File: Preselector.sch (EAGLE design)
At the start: 167 parts, among them IC4 TPS7A8101DRB, IC58 LMZ31707RVQ, Q2 FDV303N, X1 0733660061, X10 0733660061, X11 0733660061, X12 0733660061, X13 0733660061, X14 0733660061, X15 0733660061, X16 0733660061, X17 0733660061, X18 0733660061, X19 0733660061, X2 0733660061, X20 0733660061, X21 0733660061, X22 0733660061, X23 0733660061, X24 0733660061, X25 0733660061, X26 0733660061, X27 0733660061, X28 0733660061, X29 0733660061, X3 0733660061, X30 0733660061, X31 0733660061, X32 0733660061, X4 0733660061, X5 0733660061, X6 0733660061, X7 0733660061, X8 0733660061, X9 0733660061

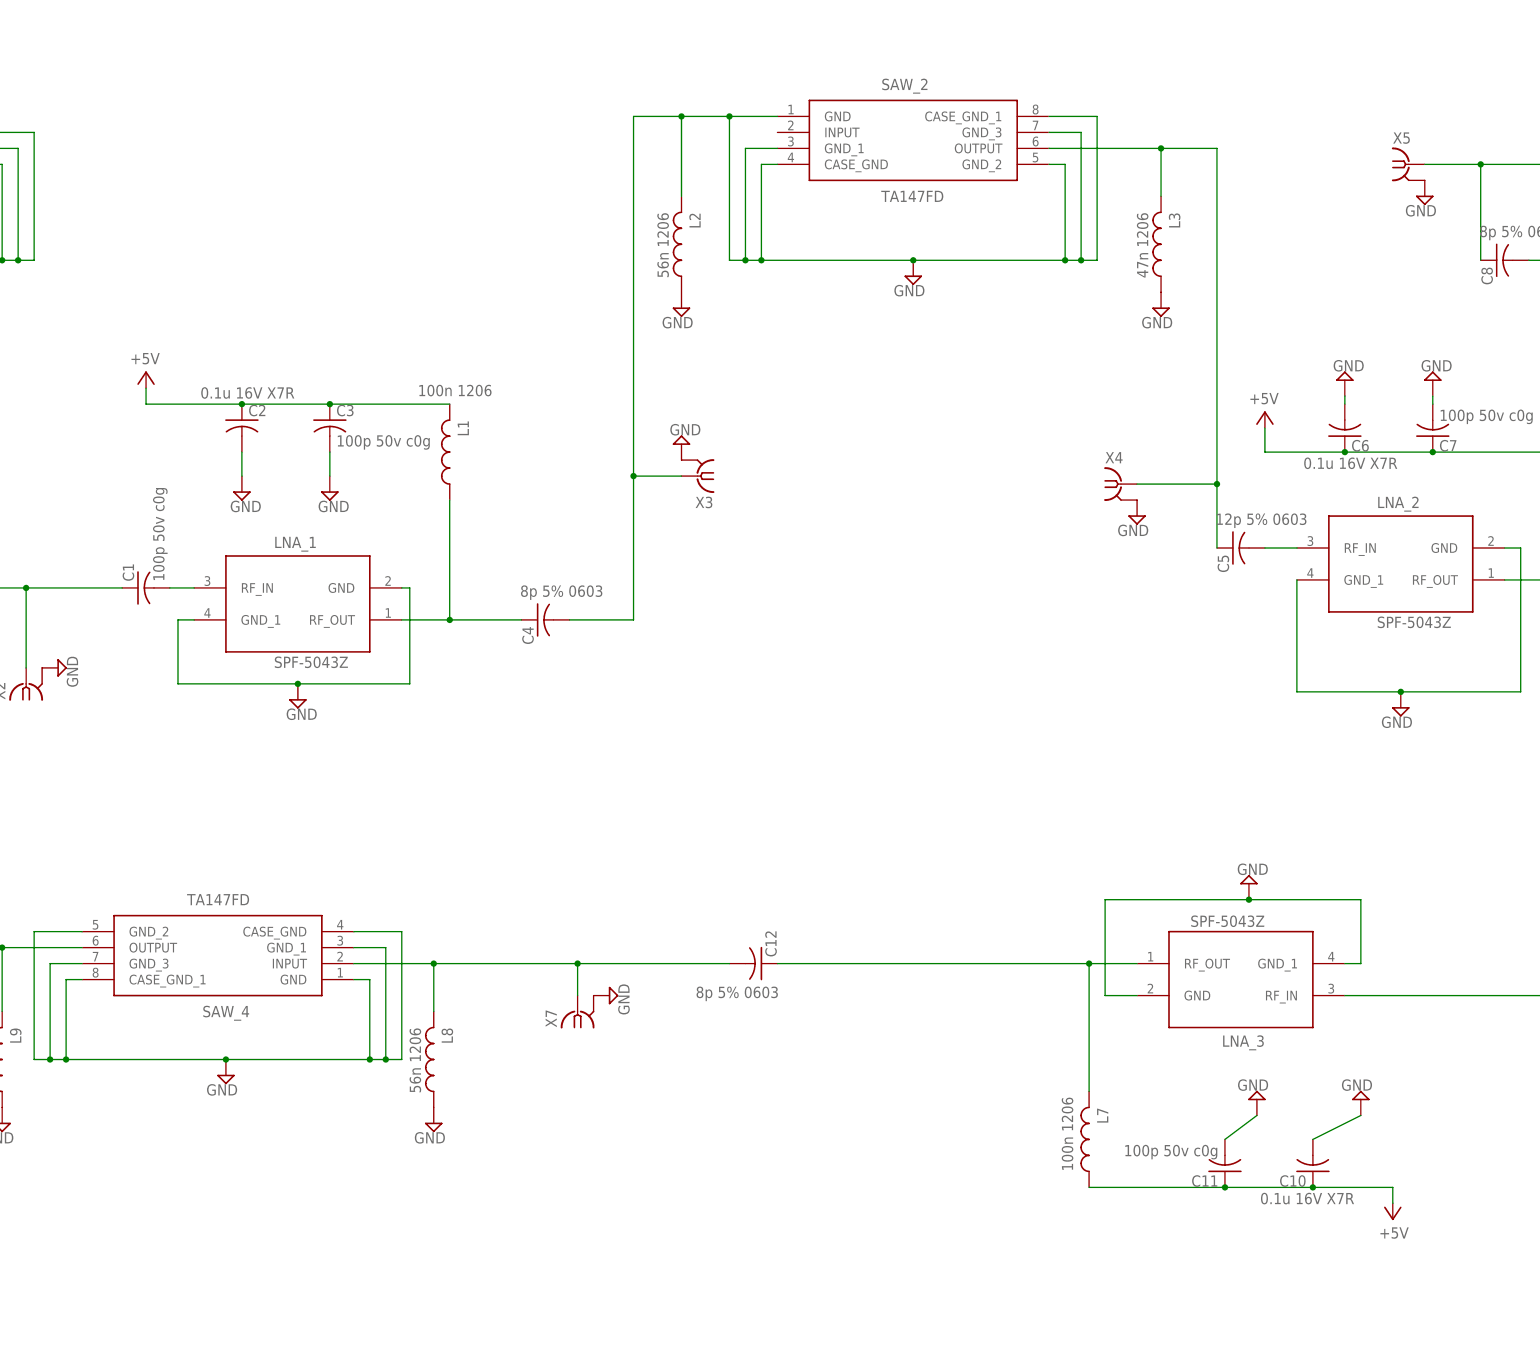
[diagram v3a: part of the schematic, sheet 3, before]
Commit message: Fixed all ERC errors
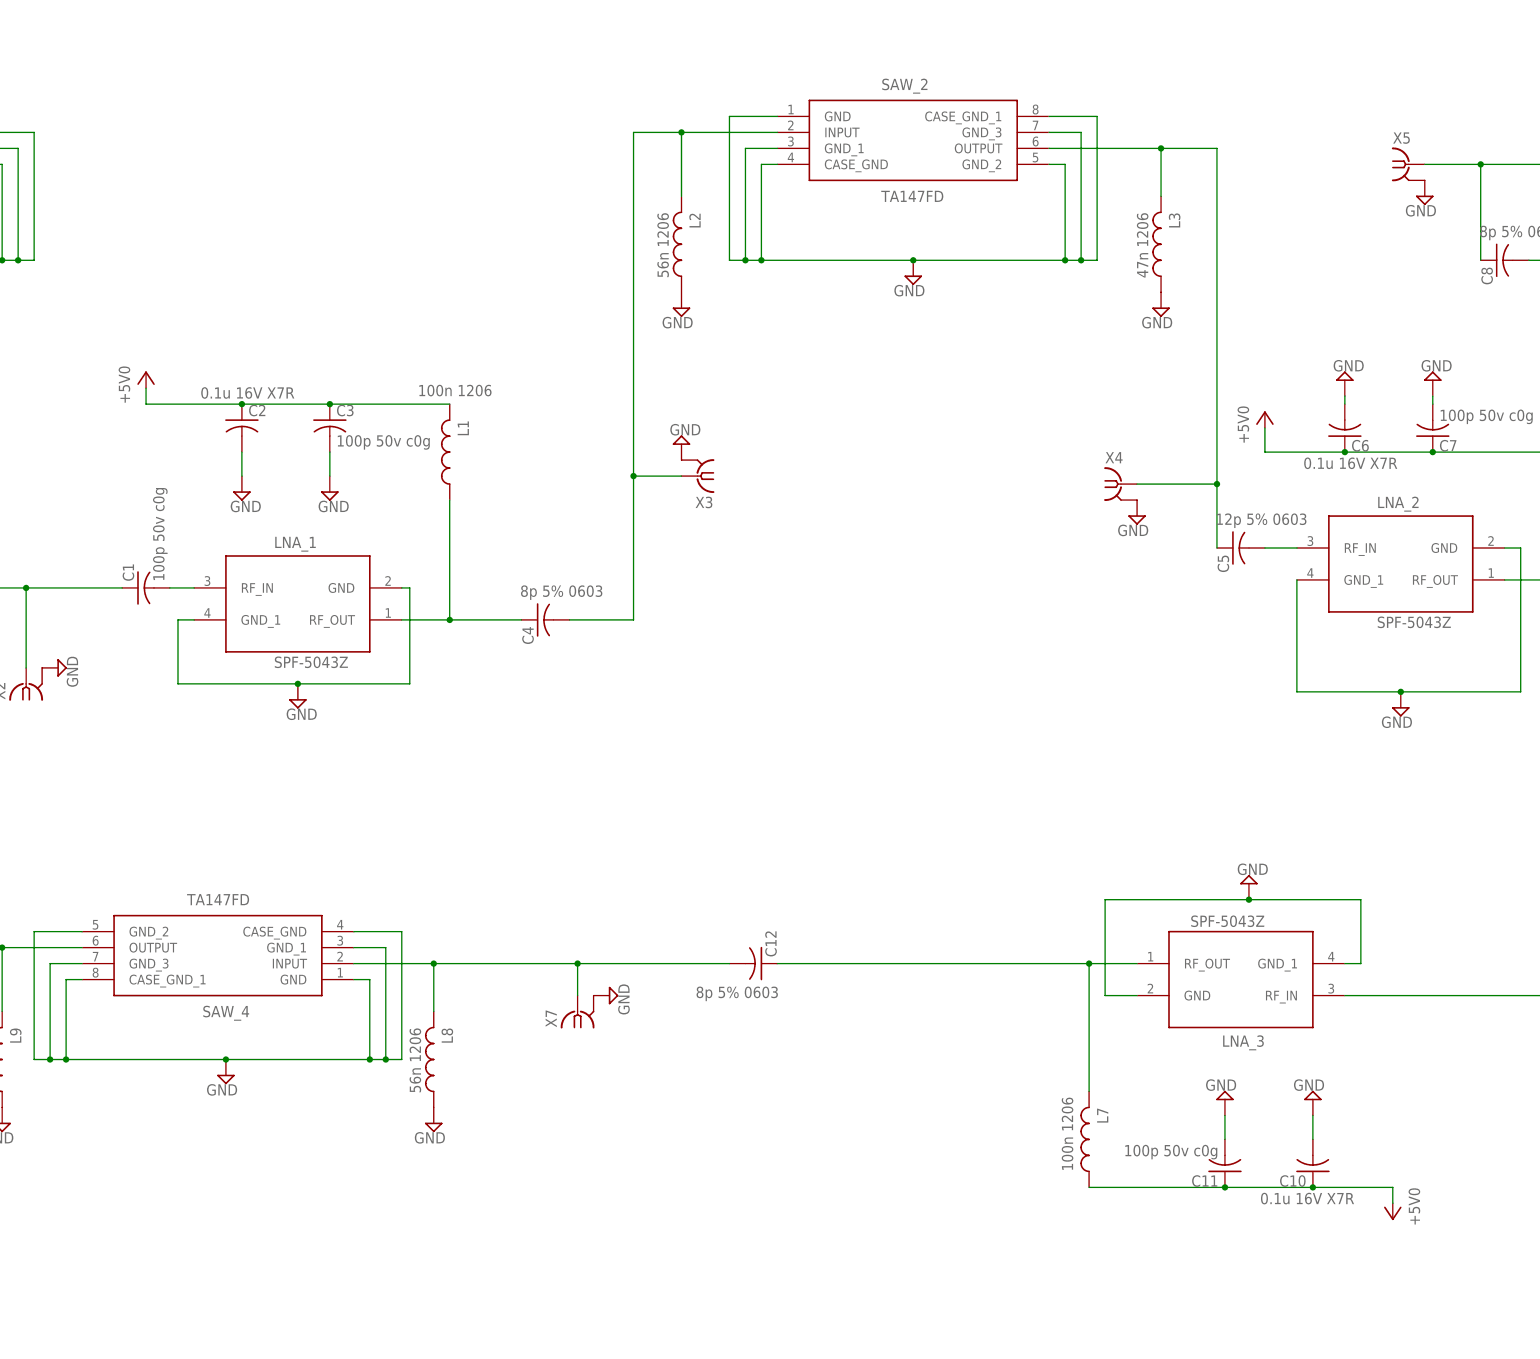
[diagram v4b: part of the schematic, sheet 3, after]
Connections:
- net +5V renamed +5V0
- net 1.25M_RF_IN1 renamed LNA_6_IN
- net 1.25M_RF_IN3 renamed LNA_5_IN
- net 2M_RF_IN1 renamed SAW_9_IN
- net 2M_RF_IN10 renamed SAW_10_OUT
- net 2M_RF_IN11 renamed SAW_11_12_RF
- net 2M_RF_IN14 renamed SAW+6_OUT
- net 2M_RF_IN15 renamed SAW_7_IN
- net 2M_RF_IN16 renamed SAW_7_8_RF
- net 2M_RF_IN17 renamed LNA_1_OUT
- net 2M_RF_IN19 renamed LNA_2_OUT
- net 2M_RF_IN2 renamed LNA_4_IN
- net 2M_RF_IN20 renamed LNA_3_OUT
- net 2M_RF_IN3 renamed 1.25_RF_OUT
- net 2M_RF_IN5 renamed SAW_10_IN
- net 2M_RF_IN6 renamed LNA_8_IN
- net 2M_RF_IN7 renamed SAW_11_IN
- net 2M_RF_IN8 renamed LNA_9_IN
- net 2M_RF_IN9 renamed SAW_9_OUT
- net 2M_RF_IN_14 renamed LNA_1_IN
- net 2M_RF_IN_4 renamed SAW_2_OUT
- net 2M_RF_IN_7 renamed SAW_3_IN
- net 2M_RF_IN_9 renamed LNA_3_IN
- net GND5 renamed LNA_8_OUT
- net GND6 renamed LNA_9_OUT
- net N$11 renamed SAW_3_OUT
- net N$13 renamed LNA_6_OUT
- net N$7 renamed 70CM_RF_OUT
- net N$9 renamed LNA_2_IN
- removed net 2M_RF_IN4: C26.1, C26.2, LNA_7.RF_IN, X17G$1.1
- new net 2M_RF_OUT: C13.2, X8G$1.1
- new net LNA_7_IN: C26.2, LNA_7.RF_IN
- new net LNA_7_OUT: C29.1, L13.1, LNA_7.RF_OUT
- new net SAW_2_IN: C4.2, L2.2, SAW_2.INPUT, X3G$1.1
- new net SAW_6_IN: C21.2, SAW_6.INPUT, X12G$1.1
- net 1.25M_RF_IN: no longer C21.1, L11.1, LNA_5.RF_OUT
- net 2M_RF_IN: no longer C13.2, X8G$1.1
- net 70CM_RF_IN: now also C26.1, X17G$1.1; no longer C29.1, L13.1, LNA_7.RF_OUT
- net GND: no longer C4.2, L2.2, X3G$1.1
- net LNA_5_OUT: now also C21.1, L11.1, LNA_5.RF_OUT; no longer C21.2, SAW_6.INPUT, X12G$1.1
- net SAW_4_IN: now also C12.2, L8.2, SAW_4.INPUT, X7G$1.1; no longer C13.1, L9.2, SAW_4.OUTPUT
- net SAW_4_OUT: now also C13.1, L9.2, SAW_4.OUTPUT; no longer C12.2, L8.2, SAW_4.INPUT, X7G$1.1

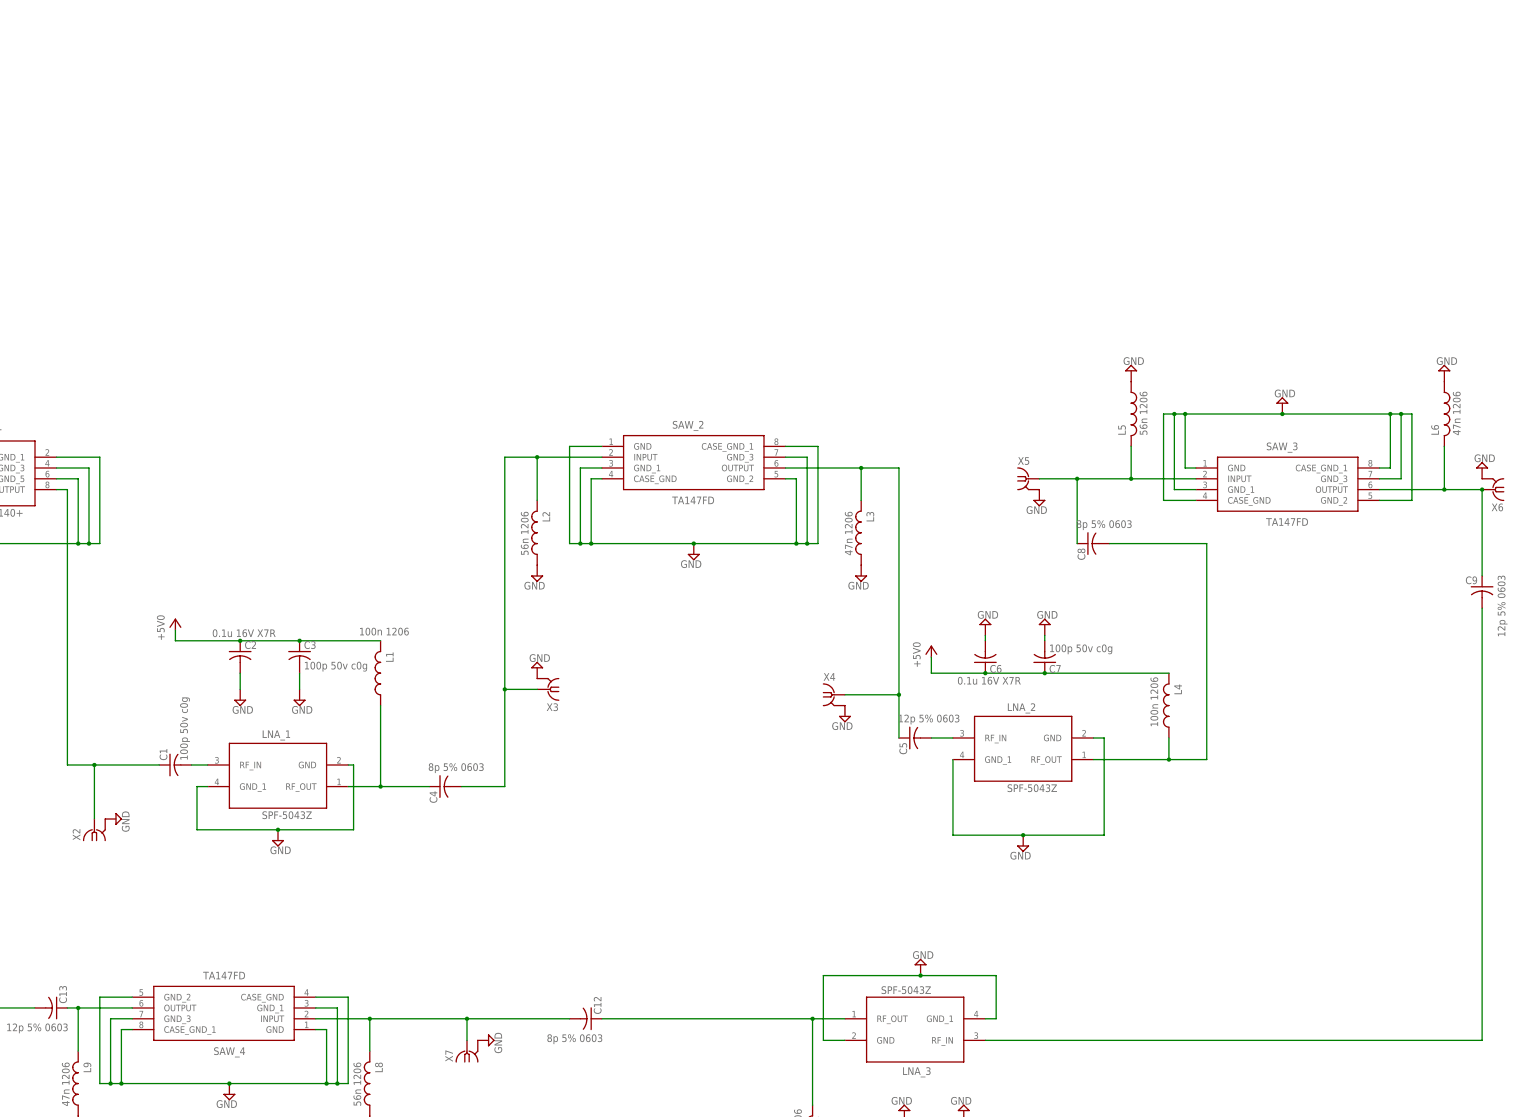
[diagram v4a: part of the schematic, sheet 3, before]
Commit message: Added first 2 LDO's on 2m band
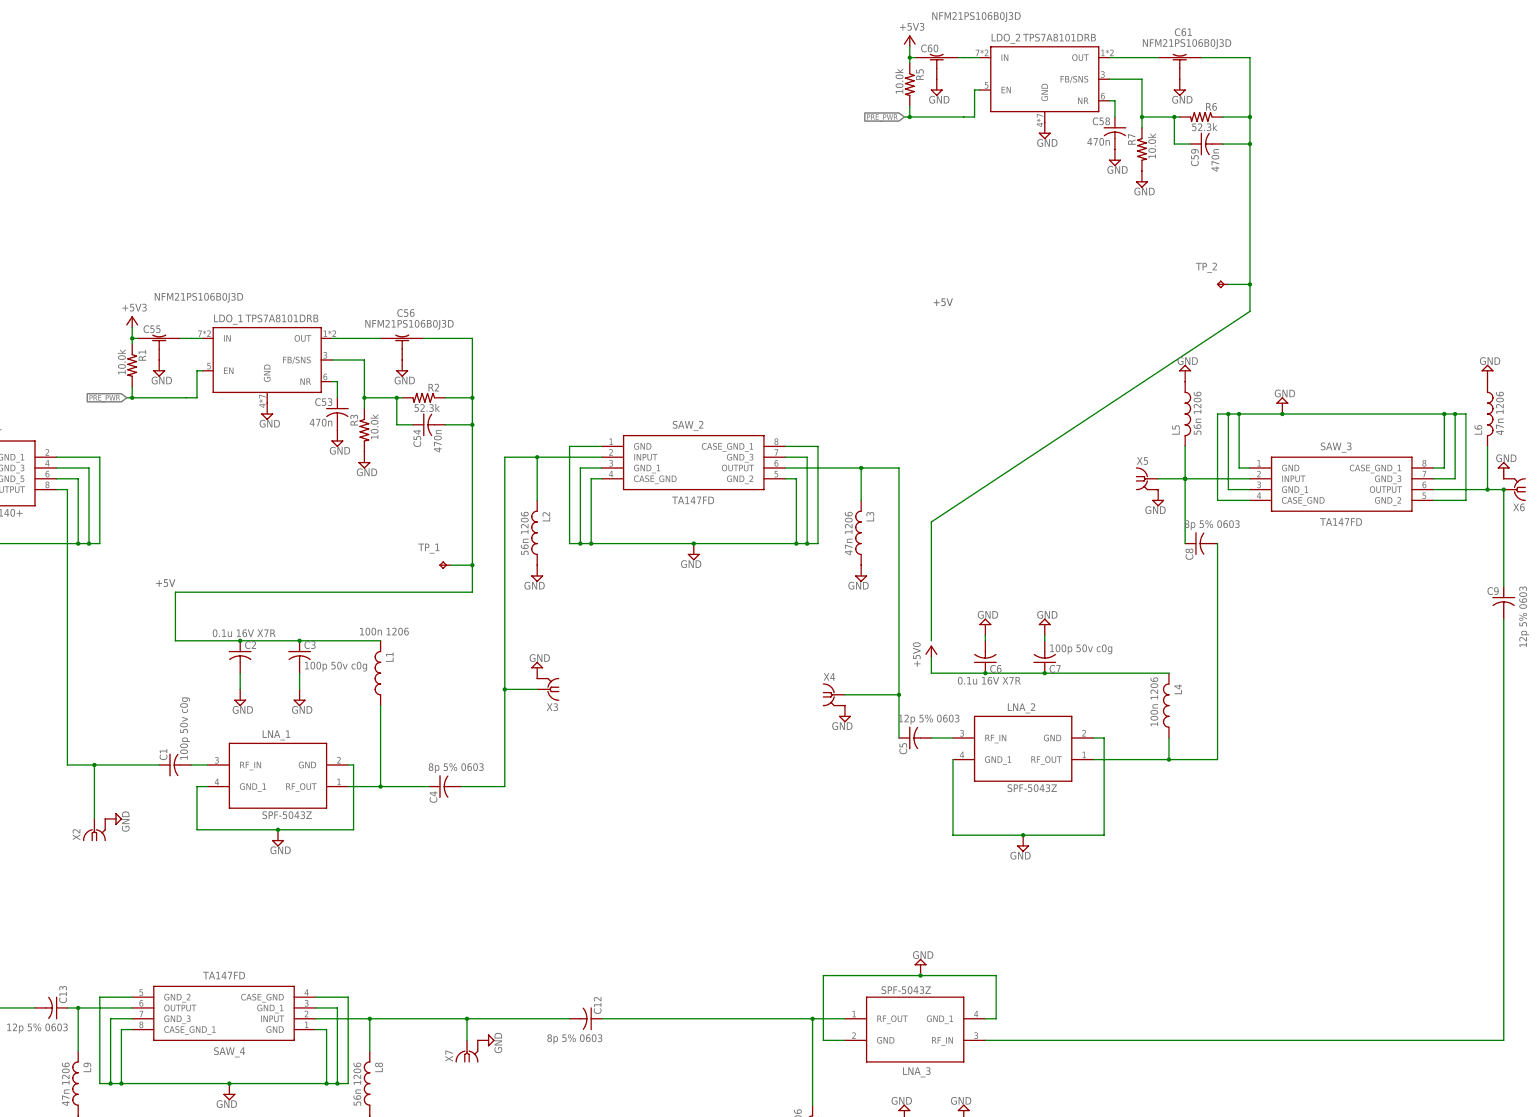
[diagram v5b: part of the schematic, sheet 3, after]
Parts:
- added C53, C54, C58, C59: 470n, rcl:C-USC0402K
- added C55, C56, C60, C61: NFM21PS106B0J3D, DEEP EDDY:NFM21PS
- added LDO_1, LDO_2: TPS7A8101DRB, DEEP EDDY:TPS7A8101DRB
- added R1, R3, R5, R7: 10.0k, rcl:R-US_R0603
- added R2, R6: 52.3k, rcl:R-US_R0603
- added TP_1, TP_2: TPTP20SQ, testpad:TPTP20SQ
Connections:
- new net LDO_1_5V: C2.1, C3.1, C54.2, C56.OUT, L1.2, R2.1, TP_1.TP
- new net LDO_1_5V1: C59.2, C61.OUT, R6.1, TP_2.TP
- new net N$12: C54.1, LDO_1.FB/SNS, R2.2, R3.1
- new net N$13: C53.1, LDO_1.NR
- new net N$14: C55.OUT, LDO_1.IN
- new net N$15: C56.IN, LDO_1.OUT
- new net N$16: C59.1, LDO_2.FB/SNS, R6.2, R7.1
- new net N$17: C58.1, LDO_2.NR
- new net N$18: C60.OUT, LDO_2.IN
- new net N$19: C61.IN, LDO_2.OUT
- net +5V0: no longer C2.1, C3.1, L1.2
- net +5V3: now also C55.IN, C60.IN, R1.1, R5.1
- net GND: now also C53.2, C55.GND, C56.GND, C58.2, C60.GND, C61.GND, LDO_1.GND, LDO_2.GND, R3.2, R7.2
- net PRE_PWR: now also LDO_1.EN, LDO_2.EN, R1.2, R5.2
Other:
- moved on the sheet: C8, C9, L5, L6, SAW_3, X5, X6
